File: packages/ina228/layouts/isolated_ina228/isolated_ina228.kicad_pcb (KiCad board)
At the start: 2 copper layers, 16.2 x 1.5 mm, 17 parts

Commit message: Update build script and regenerate outputs
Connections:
- C1 pad 1: gnd-2 -> gnd
- C1 pad 2: gnd -> gnd-2
- C2 pad 1: hv-3 -> hv-1
- C2 pad 2: gnd-2 -> gnd
- C3 pad 1: power_isolator-hv-1 -> power_isolator-hv
- C3 pad 2: gnd-2 -> gnd
- C4 pad 1: hv -> hv-4
- C4 pad 2: gnd -> gnd-2
- C5 pad 1: hv -> hv-4
- C5 pad 2: gnd -> gnd-2
- D1 pad 2: hv-2 -> hv-5
- D2 pad 2: hv -> hv-4
- L1 pad 1: hv-3 -> hv-1
- L1 pad 2: power_isolator-hv-1 -> power_isolator-hv
- L2 pad 1: hv -> hv-4
- L2 pad 2: power_isolator-hv -> power_isolator-hv-1
- R1 pad 2: gnd -> gnd-2
- R2 pad 1: hv-4 -> hv
- R2 pad 2: hv-1 -> hv-2
- R3 pad 2: gnd -> gnd-2
- R4 pad 1: line-1 -> line
- R4 pad 2: hv -> hv-4
- R5 pad 1: line-3 -> line-1
- R5 pad 2: hv -> hv-4
- U1 pad 1: hv-5 -> hv-3
- U1 pad 2: line-2 -> line-3
- U1 pad 3: line -> line-2
- U1 pad 5: gnd -> gnd-2
- U1 pad 6: line-1 -> line
- U1 pad 7: line-3 -> line-1
- U1 pad 8: hv -> hv-4
- U2 pad 1: ina228.ina288-line -> ina228.ina288-line-1
- U2 pad 10: hv-4 -> hv
- U2 pad 2: ina228.ina288-line-1 -> ina228.ina288-line
- U2 pad 3: hv-2 -> hv-5
- U2 pad 4: line-3 -> line-1
- U2 pad 5: line-1 -> line
- U2 pad 6: hv -> hv-4
- U2 pad 7: gnd -> gnd-2
- U2 pad 8: hv-4 -> hv
- U2 pad 9: hv-1 -> hv-2
- U3 pad 1: gnd-2 -> gnd
- U3 pad 2: power_isolator-hv-1 -> power_isolator-hv
- U3 pad 3: gnd -> gnd-2
- U3 pad 4: power_isolator-hv -> power_isolator-hv-1
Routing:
- net hv-4: track 8.29 -> 25.6 mm, vias 0 -> 2
- net hv: track 25.6 -> 8.29 mm, vias 2 -> 0
- net line-3: track 6.52 -> 0.00 mm
- net power_isolator-hv-1: track 8.56 -> 2.96 mm
- net power_isolator-hv: track 2.96 -> 8.56 mm
- net hv-5: track 0.00 -> 5.18 mm
- net line: track 0.00 -> 4.71 mm
- net hv-1: track 5.38 -> 1.88 mm
- net hv-3: track 1.88 -> 0.00 mm
- net line-1: track 4.71 -> 6.52 mm
- added copper zone on B.Cu, net gnd-2
- removed copper zone on B.Cu, net gnd

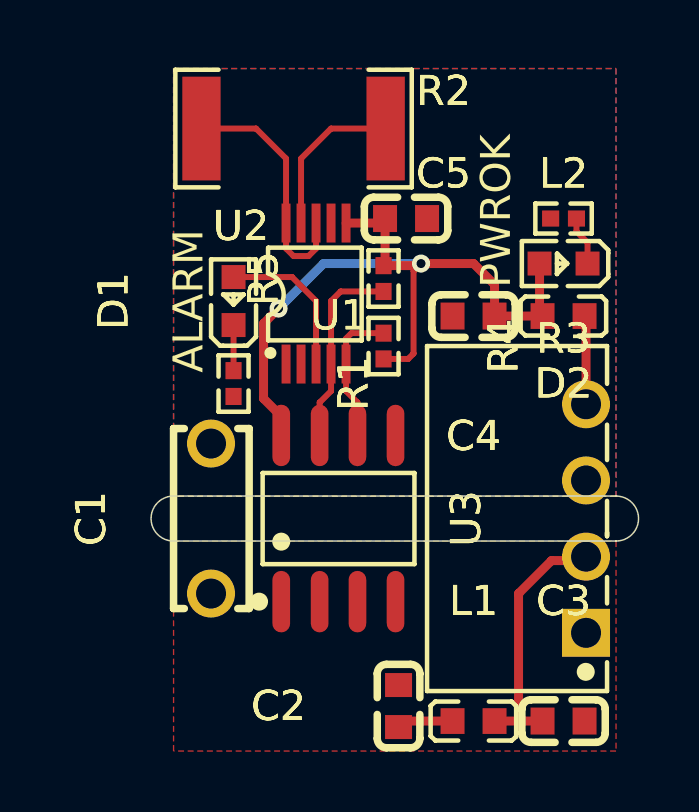
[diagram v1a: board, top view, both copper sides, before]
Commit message: Build all packages without designators on silkscreen.
Also disable fail_on_drc and enable keep_picked_parts for build
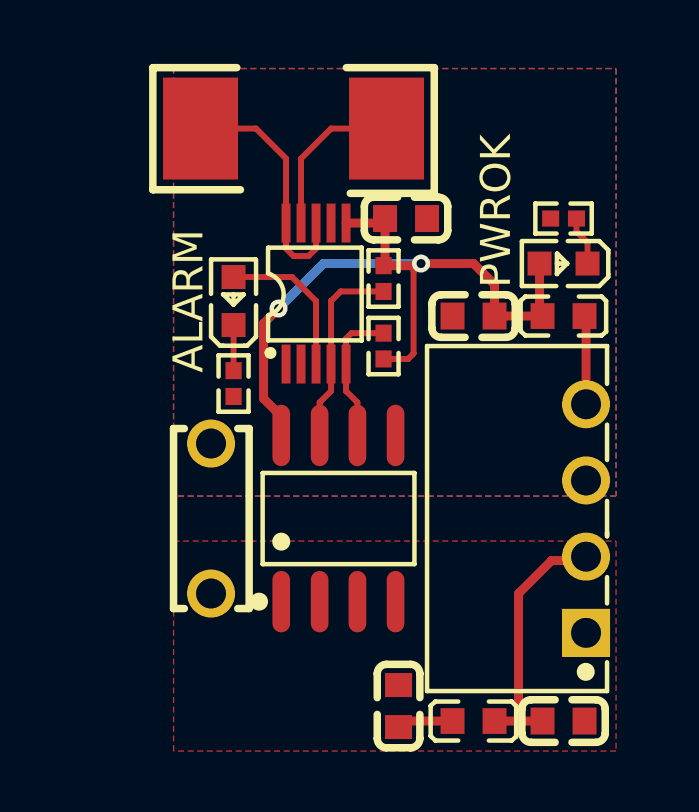
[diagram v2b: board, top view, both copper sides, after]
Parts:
- C4: value 10µF ±20% 6.3V X5R -> 10µF ±10% 10V X5R
- R2: footprint atopile:R2512-78e9bd -> atopile:RES-SMD_L6.4-W3.2-1-4e2b76
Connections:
- C1 pad 1: gnd -> gnd-1
- C1 pad 2: gnd-2 -> gnd
- C2 pad 1: hv-1 -> hv-4
- C2 pad 2: gnd -> gnd-1
- C3 pad 2: gnd -> gnd-1
- C4 pad 1: hv-4 -> hv-1
- C4 pad 2: gnd-2 -> gnd
- C5 pad 1: hv-4 -> hv-1
- C5 pad 2: gnd-2 -> gnd
- D1 pad 2: hv-5 -> hv
- D2 pad 2: hv-4 -> hv-1
- L1 pad 1: hv-1 -> hv-4
- L2 pad 1: hv-4 -> hv-1
- R1 pad 2: gnd-2 -> gnd
- R2 pad 1: hv -> hv-3
- R2 pad 2: hv-2 -> hv-5
- R3 pad 2: gnd-2 -> gnd
- R4 pad 1: line -> line-2
- R4 pad 2: hv-4 -> hv-1
- R5 pad 1: line-1 -> line-3
- R5 pad 2: hv-4 -> hv-1
- U1 pad 1: hv-3 -> hv-2
- U1 pad 2: line-3 -> line-1
- U1 pad 3: line-2 -> line
- U1 pad 4: gnd-1 -> gnd-2
- U1 pad 5: gnd-2 -> gnd
- U1 pad 6: line -> line-2
- U1 pad 7: line-1 -> line-3
- U1 pad 8: hv-4 -> hv-1
- U2 pad 10: hv -> hv-3
- U2 pad 3: hv-5 -> hv
- U2 pad 4: line-1 -> line-3
- U2 pad 5: line -> line-2
- U2 pad 6: hv-4 -> hv-1
- U2 pad 7: gnd-2 -> gnd
- U2 pad 8: hv -> hv-3
- U2 pad 9: hv-2 -> hv-5
- U3 pad 1: gnd -> gnd-1
- U3 pad 3: gnd-2 -> gnd
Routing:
- net hv-4: track 25.6 -> 1.88 mm, vias 2 -> 0
- net hv-1: track 1.88 -> 25.6 mm, vias 0 -> 2
- net hv-3: track 0.00 -> 8.29 mm
- net line-3: track 0.00 -> 6.52 mm
- net line-1: track 6.52 -> 0.00 mm
- net hv-2: track 5.38 -> 0.00 mm
- net line-2: track 0.00 -> 4.71 mm
- net line: track 4.71 -> 0.00 mm
- net hv: track 8.29 -> 5.18 mm
- added copper zone on B.Cu, net gnd
- added copper zone on F.Cu, net gnd-1
- removed copper zone on B.Cu, net gnd-2
- removed copper zone on F.Cu, net gnd-2
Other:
- board outline removed
- board text added: "Adviced cutout"

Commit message: [Publish] Fix image links and rebuild
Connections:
- C1 pad 2: gnd -> gnd-2
- C2 pad 1: hv-4 -> hv-2
- C3 pad 1: power_isolator-hv -> power_isolator-hv-1
- C4 pad 2: gnd -> gnd-2
- C5 pad 2: gnd -> gnd-2
- L1 pad 1: hv-4 -> hv-2
- L1 pad 2: power_isolator-hv -> power_isolator-hv-1
- L2 pad 2: power_isolator-hv-1 -> power_isolator-hv
- R1 pad 2: gnd -> gnd-2
- R2 pad 2: hv-5 -> hv-4
- R3 pad 2: gnd -> gnd-2
- R4 pad 1: line-2 -> line
- R5 pad 1: line-3 -> line-2
- U1 pad 1: hv-2 -> hv-5
- U1 pad 3: line -> line-3
- U1 pad 4: gnd-2 -> gnd
- U1 pad 5: gnd -> gnd-2
- U1 pad 6: line-2 -> line
- U1 pad 7: line-3 -> line-2
- U2 pad 4: line-3 -> line-2
- U2 pad 5: line-2 -> line
- U2 pad 7: gnd -> gnd-2
- U2 pad 9: hv-5 -> hv-4
- U3 pad 2: power_isolator-hv -> power_isolator-hv-1
- U3 pad 3: gnd -> gnd-2
- U3 pad 4: power_isolator-hv-1 -> power_isolator-hv
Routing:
- net line-3: track 6.52 -> 0.00 mm
- net power_isolator-hv-1: track 2.96 -> 8.56 mm
- net power_isolator-hv: track 8.56 -> 2.96 mm
- net hv-5: track 5.38 -> 0.00 mm
- net line: track 0.00 -> 4.71 mm
- net hv-4: track 1.88 -> 5.38 mm
- net hv-2: track 0.00 -> 1.88 mm
- net line-2: track 4.71 -> 6.52 mm
- added copper zone on B.Cu, net gnd-2
- added copper zone on F.Cu, net gnd-2
- removed copper zone on B.Cu, net gnd
- removed copper zone on F.Cu, net gnd
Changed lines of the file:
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@@
     )
     (net 0 "")
-    (net 1 "line-3")
+    (net 1 "line-2")
     (net 2 "hv-3")
-    (net 3 "gnd")
-    (net 4 "line-2")
-    (net 5 "power_isolator-hv-1")
-    (net 6 "hv-2")
+    (net 3 "gnd-2")
+    (net 4 "line")
+    (net 5 "power_isolator-hv")
+    (net 6 "hv-5")
     (net 7 "hv")
     (net 8 "alarm_led.led-cathode")
-    (net 9 "gnd-2")
+    (net 9 "gnd")
     (net 10 "power_indicator-cathode")
-    (net 11 "hv-4")
-    (net 12 "power_isolator-hv")
+    (net 11 "hv-2")
+    (net 12 "power_isolator-hv-1")
     (net 13 "hv-1")
-    (net 14 "line")
-    (net 15 "hv-5")
+    (net 14 "line-3")
+    (net 15 "hv-4")
     (net 16 "ina228.ina288-line")
     (net 17 "ina228.ina288-line-1")
@@
             (size 0.3 1.3)
             (layers "F.Cu" "F.Mask" "F.Paste")
-            (net 1 "line-3")
+            (net 1 "line-2")
         )
         (pad "5" smd rect
@@
             (size 0.3 1.3)
             (layers "F.Cu" "F.Mask" "F.Paste")
-            (net 4 "line-2")
+            (net 4 "line")
         )
         (pad "6" smd rect
@@
             (size 0.3 1.3)
             (layers "F.Cu" "F.Mask" "F.Paste")
-            (net 3 "gnd")
+            (net 3 "gnd-2")
         )
         (pad "8" smd rect
@@
             (size 0.3 1.3)
             (layers "F.Cu" "F.Mask" "F.Paste")
-            (net 15 "hv-5")
+            (net 15 "hv-4")
         )
         (pad "10" smd rect
@@
             (size 0.57 0.54)
             (layers "F.Cu" "F.Mask" "F.Paste")
-            (net 1 "line-3")
+            (net 1 "line-2")
         )
         (pad "2" smd rect
@@
             (size 0.59 2.05)
             (layers "F.Cu" "F.Mask" "F.Paste")
-            (net 6 "hv-2")
+            (net 6 "hv-5")
         )
         (pad "2" smd oval
@@
             (size 0.59 2.05)
             (layers "F.Cu" "F.Mask" "F.Paste")
-            (net 14 "line")
+            (net 14 "line-3")
         )
         (pad "4" smd oval
@@
             (size 0.59 2.05)
             (layers "F.Cu" "F.Mask" "F.Paste")
-            (net 9 "gnd-2")
+            (net 9 "gnd")
         )
         (pad "5" smd oval
@@
             (size 0.59 2.05)
             (layers "F.Cu" "F.Mask" "F.Paste")
-            (net 3 "gnd")
+            (net 3 "gnd-2")
         )
         (pad "6" smd oval
@@
             (size 0.59 2.05)
             (layers "F.Cu" "F.Mask" "F.Paste")
-            (net 4 "line-2")
+            (net 4 "line")
         )
         (pad "7" smd oval
@@
             (size 0.59 2.05)
             (layers "F.Cu" "F.Mask" "F.Paste")
-            (net 1 "line-3")
+            (net 1 "line-2")
         )
         (pad "8" smd oval
@@
             (size 0.8 0.86)
             (layers "F.Cu" "F.Mask" "F.Paste")
-            (net 5 "power_isolator-hv-1")
+            (net 5 "power_isolator-hv")
         )
         (embedded_fonts no)
@@
             (size 0.8 0.9)
             (layers "F.Cu" "F.Mask" "F.Paste")
-            (net 11 "hv-4")
+            (net 11 "hv-2")
         )
         (pad "2" smd rect
@@
             (size 0.8 0.86)
             (layers "F.Cu" "F.Mask" "F.Paste")
-            (net 11 "hv-4")
+            (net 11 "hv-2")
         )
         (pad "2" smd rect
@@
             (size 0.8 0.86)
             (layers "F.Cu" "F.Mask" "F.Paste")
-            (net 12 "power_isolator-hv")
+            (net 12 "power_isolator-hv-1")
         )
         (embedded_fonts no)
@@
             (size 0.8 0.9)
             (layers "F.Cu" "F.Mask" "F.Paste")
-            (net 12 "power_isolator-hv")
+            (net 12 "power_isolator-hv-1")
         )
         (pad "2" smd rect
@@
             (size 0.57 0.54)
             (layers "F.Cu" "F.Mask" "F.Paste")
-            (net 3 "gnd")
+            (net 3 "gnd-2")
         )
         (embedded_fonts no)
@@
             (size 0.57 0.54)
             (layers "F.Cu" "F.Mask" "F.Paste")
-            (net 4 "line-2")
+            (net 4 "line")
         )
         (pad "2" smd rect
@@
             (drill 0.999998)
             (layers "*.Cu" "*.Mask")
-            (net 3 "gnd")
+            (net 3 "gnd-2")
             (remove_unused_layers no)
         )
@@
             (size 0.8 0.9)
             (layers "F.Cu" "F.Mask" "F.Paste")
-            (net 3 "gnd")
+            (net 3 "gnd-2")
         )
         (embedded_fonts no)
@@
             (size 0.8 0.9)
             (layers "F.Cu" "F.Mask" "F.Paste")
-            (net 3 "gnd")
+            (net 3 "gnd-2")
         )
         (embedded_fonts no)
@@
             (size 2.5 3.4)
             (layers "F.Cu" "F.Mask" "F.Paste")
-            (net 15 "hv-5")
+            (net 15 "hv-4")
         )
         (embedded_fonts no)
@@
             (size 0.57 0.54)
             (layers "F.Cu" "F.Mask" "F.Paste")
-            (net 3 "gnd")
+            (net 3 "gnd-2")
         )
         (embedded_fonts no)
@@
             (drill 0.999998)
             (layers "*.Cu" "*.Mask")
-            (net 12 "power_isolator-hv")
+            (net 12 "power_isolator-hv-1")
             (remove_unused_layers no)
         )
@@
             (drill 0.999998)
             (layers "*.Cu" "*.Mask")
-            (net 3 "gnd")
+            (net 3 "gnd-2")
             (remove_unused_layers no)
         )
@@
             (drill 0.999998)
             (layers "*.Cu" "*.Mask")
-            (net 5 "power_isolator-hv-1")
+            (net 5 "power_isolator-hv")
             (remove_unused_layers no)
         )
@@
     (zone
         (net 3)
-        (net_name "gnd")
+        (net_name "gnd-2")
         (layers "F.Cu" "B.Cu")
         (name "Isolated GND")
